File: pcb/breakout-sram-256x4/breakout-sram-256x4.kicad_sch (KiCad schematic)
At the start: 16 parts, among them U1 IS61WV25616-10TLI, U2 IS61WV25616-10TLI, U3 IS61WV25616-10TLI, U4 IS61WV25616-10TLI

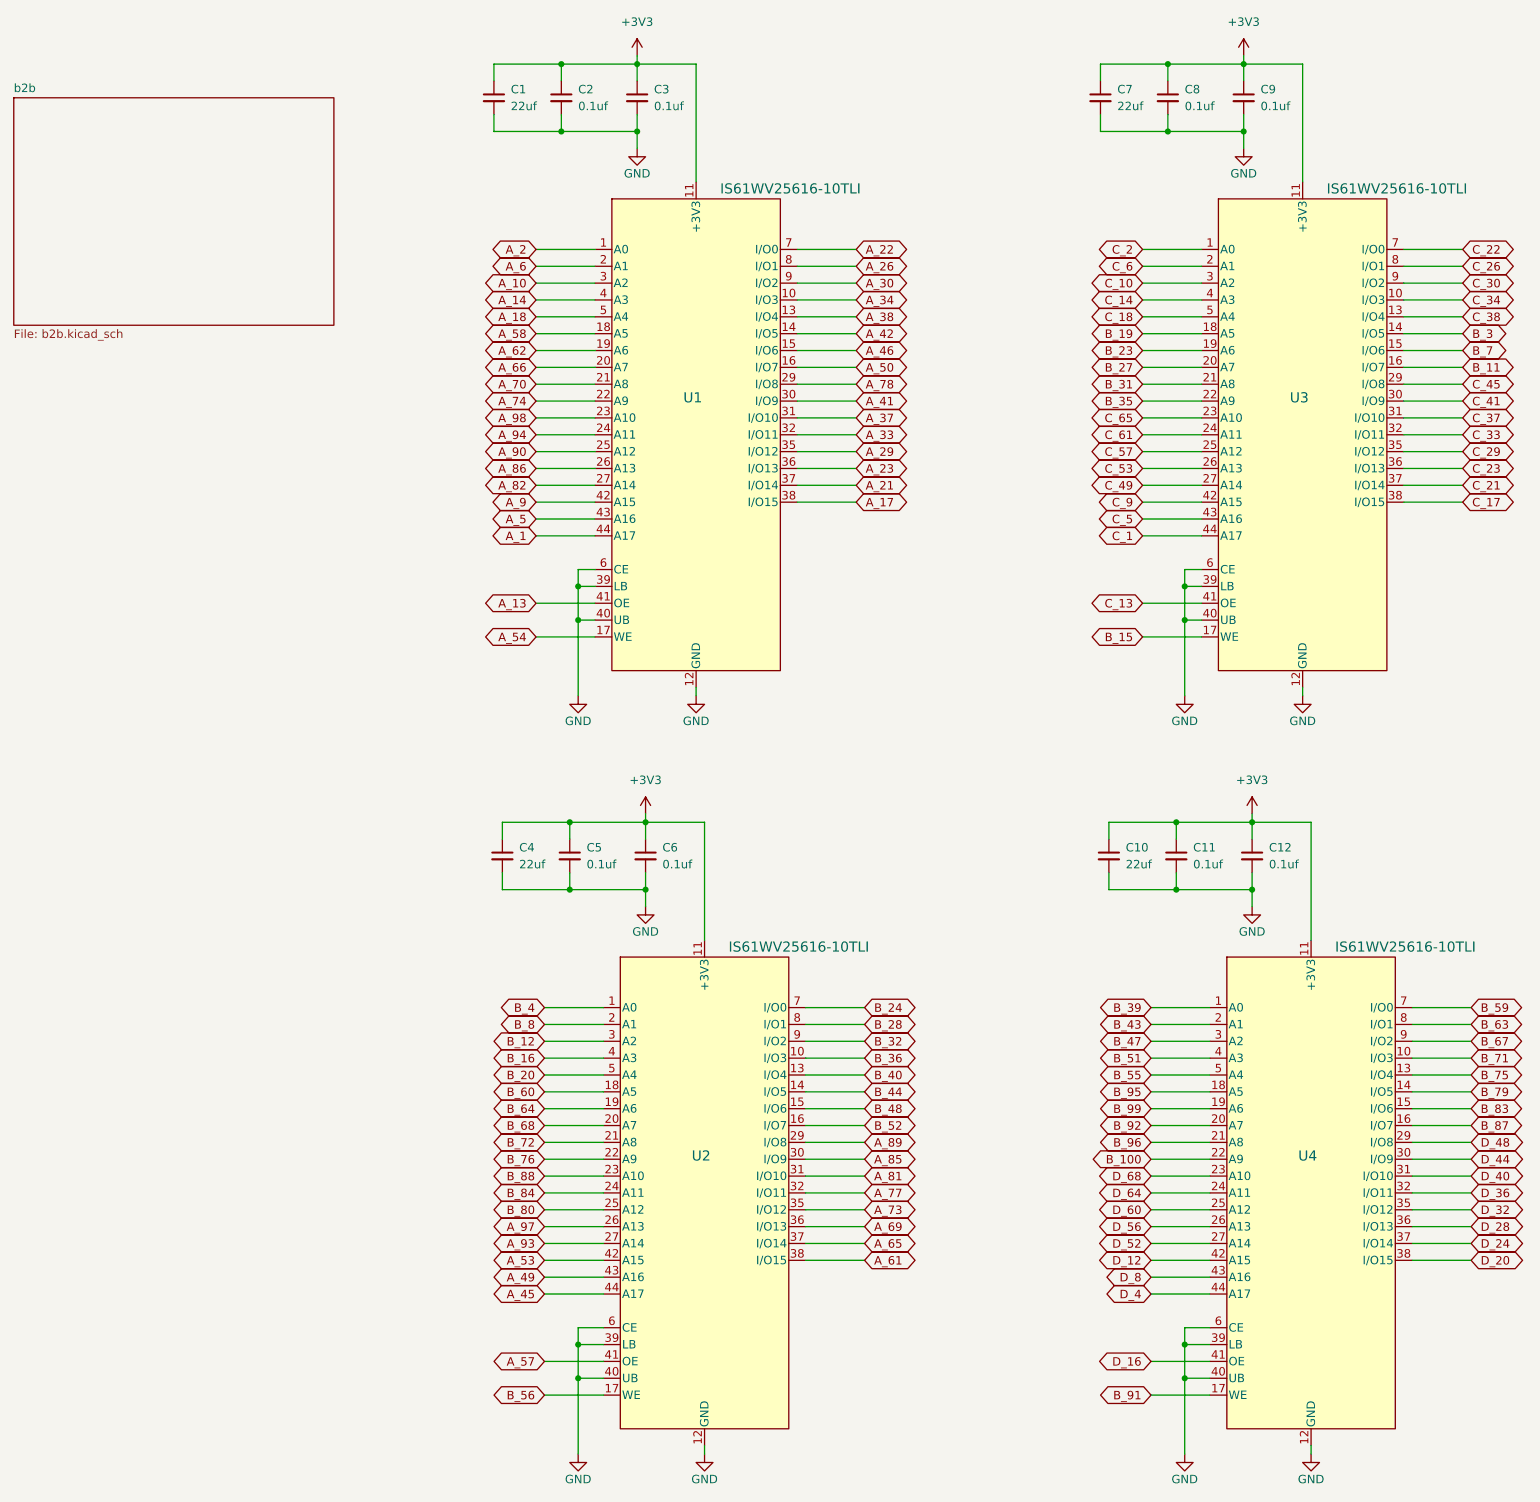
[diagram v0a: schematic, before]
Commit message: [sram_4x][pcb] make each sram ce settable with 0 ohm 603s
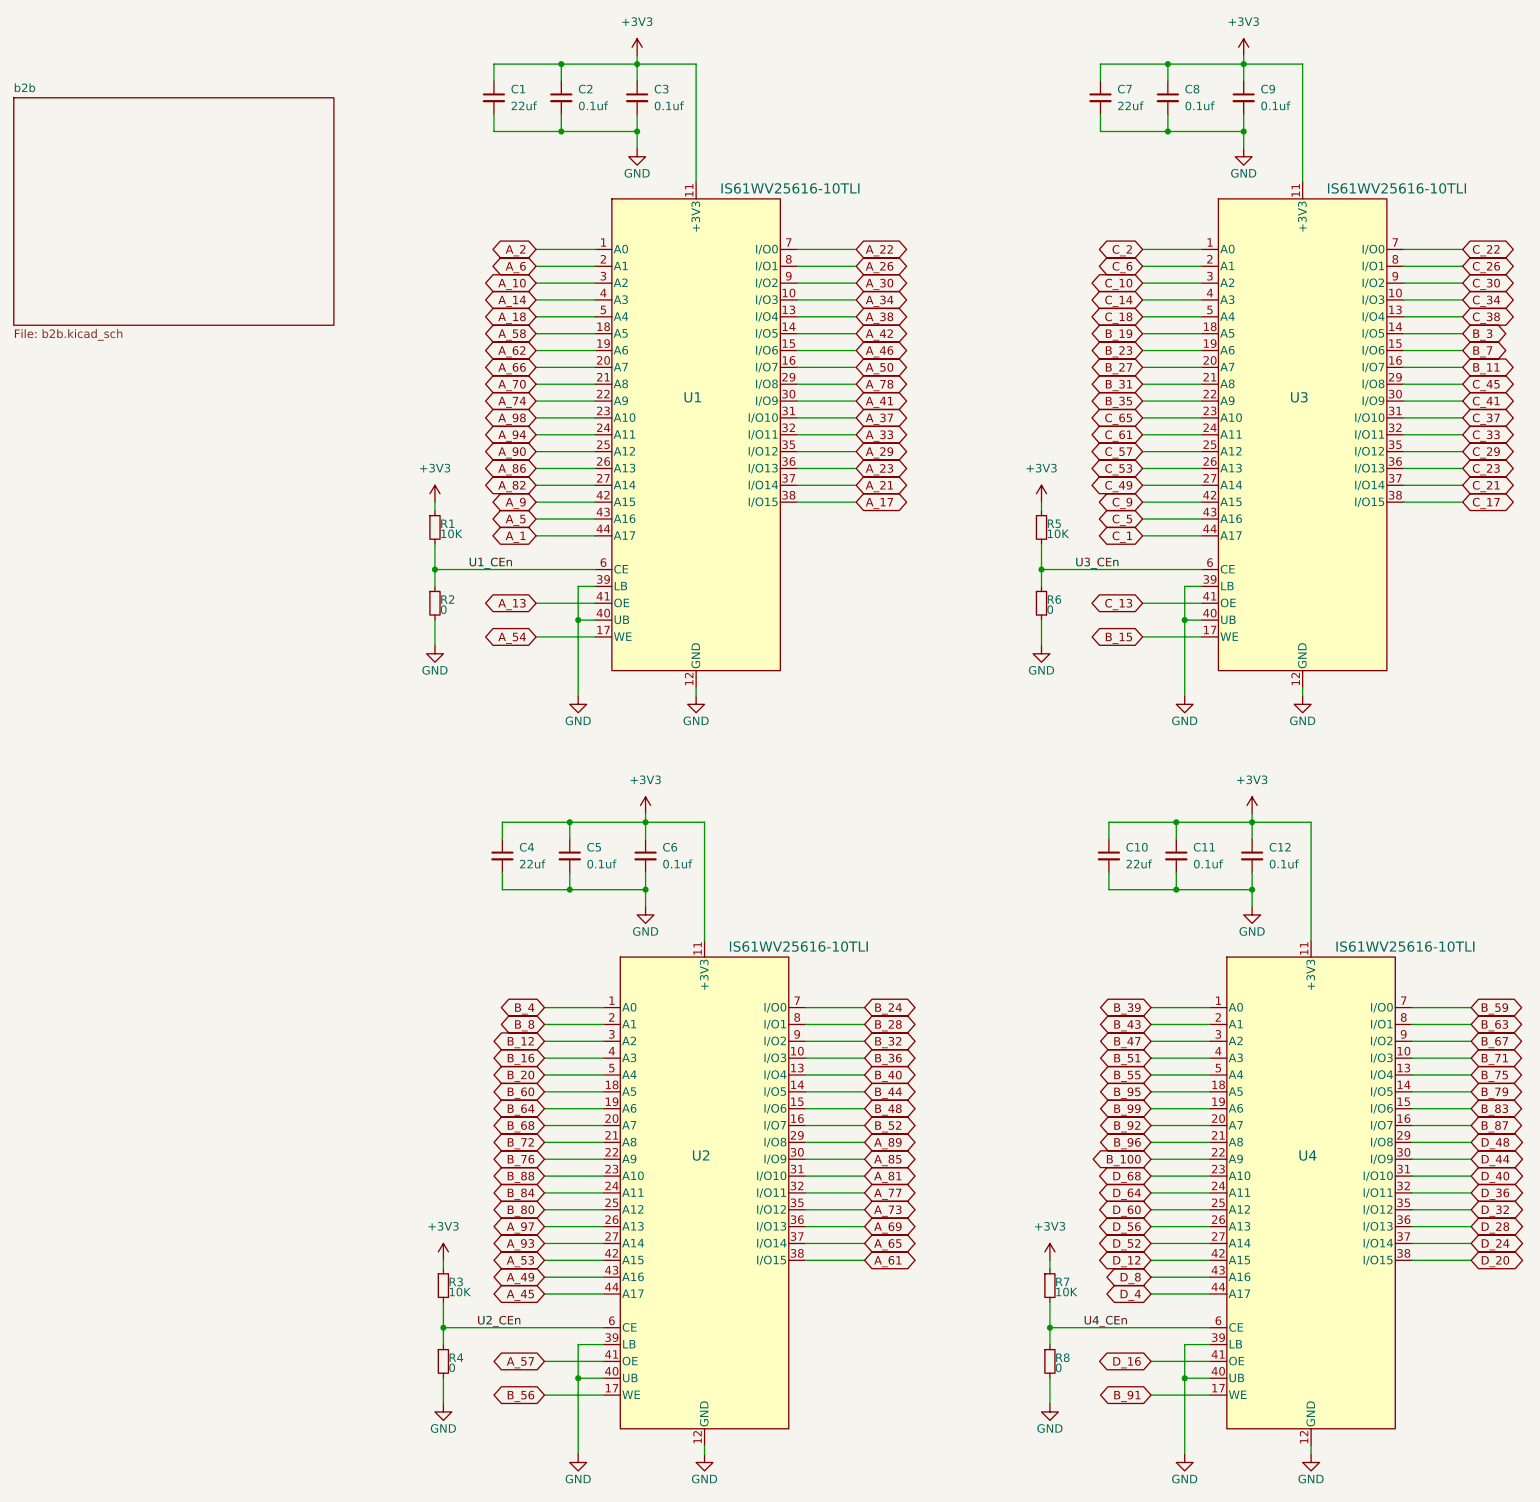
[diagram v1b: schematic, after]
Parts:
- added R1, R3, R5, R7: 10K, Resistor_SMD:R_0603_1608Metric, symbol Device:R_Small
- added R2, R4, R6, R8: 0, Resistor_SMD:R_0603_1608Metric, symbol Device:R_Small
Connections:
- net +3V3: now also R1.1, R3.1, R5.1, R7.1
- net GND: now also R2.2, R4.2, R6.2, R8.2; no longer U1.6 (CE), U2.6 (CE), U3.6 (CE), U4.6 (CE)
- new net U1_CEn: R1.2, R2.1, U1.6 (CE)
- new net U2_CEn: R3.2, R4.1, U2.6 (CE)
- new net U3_CEn: R5.2, R6.1, U3.6 (CE)
- new net U4_CEn: R7.2, R8.1, U4.6 (CE)

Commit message: [sram_4x][pcb] do not use nc from ice40
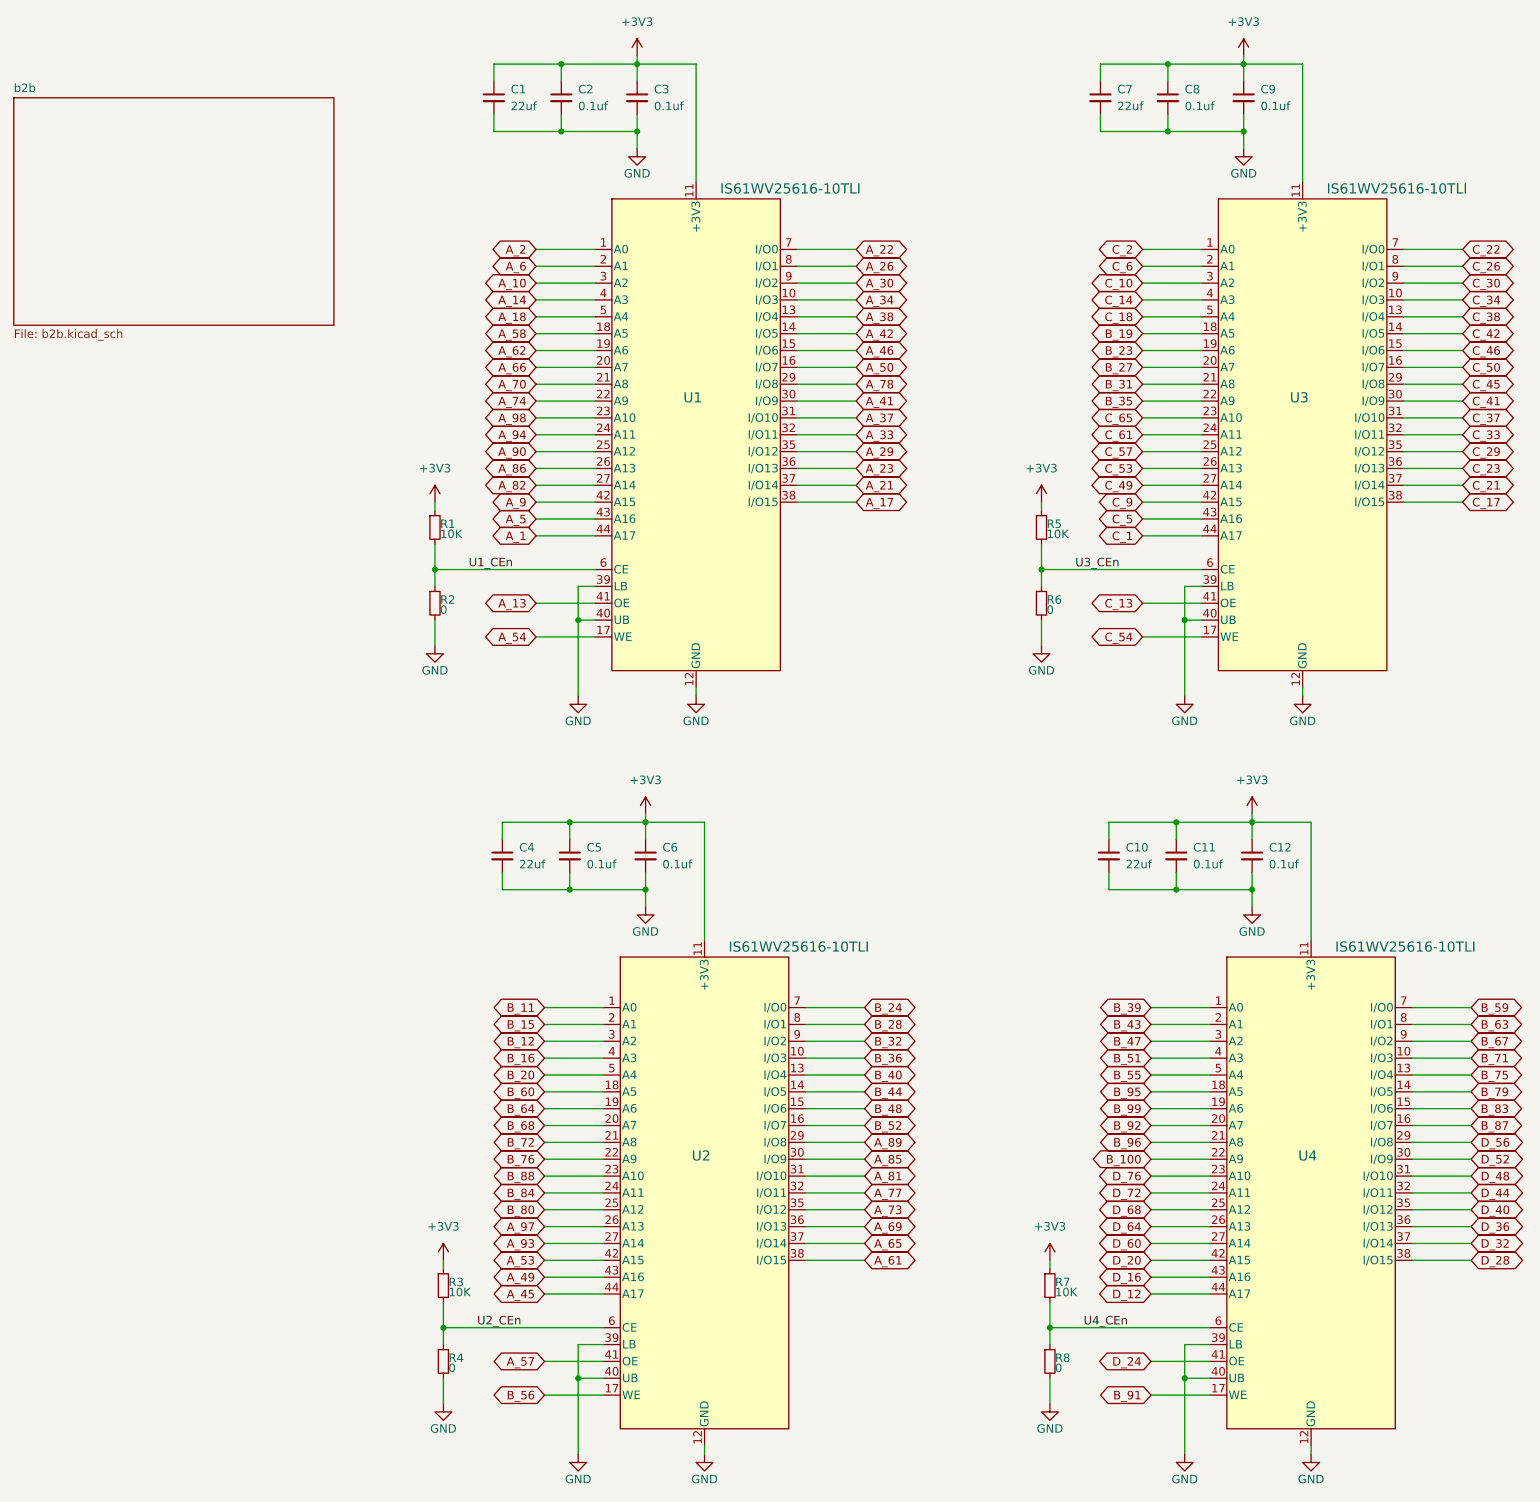
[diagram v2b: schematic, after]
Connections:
- net B_4 is gone; now on net B_11: U2.1 (A0)
- net B_8 is gone; now on net B_15: U2.2 (A1)
- net D_4 is gone; now on net D_12: U4.44 (A17)
- net D_8 is gone; now on net D_16: U4.43 (A16)
- net B_11: no longer U3.16 (I/O7)
- net B_15: no longer U3.17 (WE)
- net D_12: no longer U4.42 (A15)
- net D_16: no longer U4.41 (OE)
- net D_20: now also U4.42 (A15); no longer U4.38 (I/O15)
- net D_24: now also U4.41 (OE); no longer U4.37 (I/O14)
- net D_28: now also U4.38 (I/O15); no longer U4.36 (I/O13)
- net D_32: now also U4.37 (I/O14); no longer U4.35 (I/O12)
- net D_36: now also U4.36 (I/O13); no longer U4.32 (I/O11)
- net D_40: now also U4.35 (I/O12); no longer U4.31 (I/O10)
- net D_44: now also U4.32 (I/O11); no longer U4.30 (I/O9)
- net D_48: now also U4.31 (I/O10); no longer U4.29 (I/O8)
- net D_52: now also U4.30 (I/O9); no longer U4.27 (A14)
- net D_56: now also U4.29 (I/O8); no longer U4.26 (A13)
- net D_60: now also U4.27 (A14); no longer U4.25 (A12)
- net D_64: now also U4.26 (A13); no longer U4.24 (A11)
- net D_68: now also U4.25 (A12); no longer U4.23 (A10)
- net B_3 renamed C_42
- net B_7 renamed C_46
- new net C_50: U3.16 (I/O7)
- new net C_54: U3.17 (WE)
- new net D_72: U4.24 (A11)
- new net D_76: U4.23 (A10)

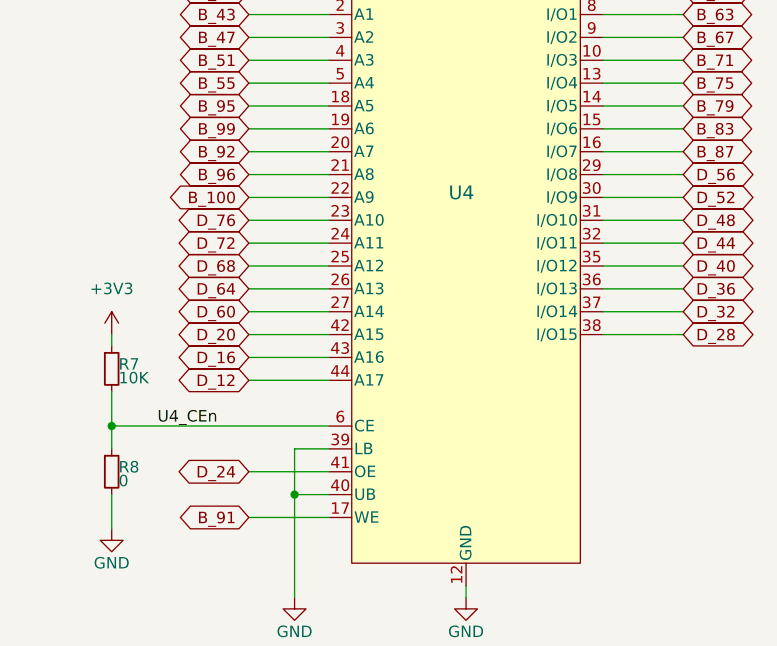
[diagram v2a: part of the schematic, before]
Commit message: [sram_4x][pcb] use bottom of lower right bank
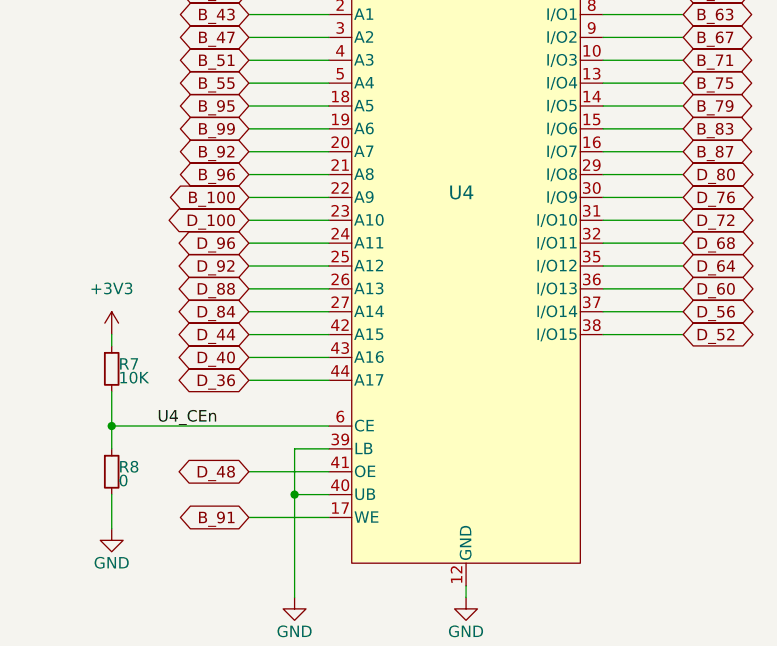
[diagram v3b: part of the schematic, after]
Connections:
- net D_12 is gone; now on net D_36: U4.44 (A17)
- net D_16 is gone; now on net D_40: U4.43 (A16)
- net D_20 is gone; now on net D_44: U4.42 (A15)
- net D_24 is gone; now on net D_48: U4.41 (OE)
- net D_28 is gone; now on net D_52: U4.38 (I/O15)
- net D_32 is gone; now on net D_56: U4.37 (I/O14)
- net D_36: no longer U4.36 (I/O13)
- net D_40: no longer U4.35 (I/O12)
- net D_44: no longer U4.32 (I/O11)
- net D_48: no longer U4.31 (I/O10)
- net D_52: no longer U4.30 (I/O9)
- net D_56: no longer U4.29 (I/O8)
- net D_60: now also U4.36 (I/O13); no longer U4.27 (A14)
- net D_64: now also U4.35 (I/O12); no longer U4.26 (A13)
- net D_68: now also U4.32 (I/O11); no longer U4.25 (A12)
- net D_72: now also U4.31 (I/O10); no longer U4.24 (A11)
- net D_76: now also U4.30 (I/O9); no longer U4.23 (A10)
- new net D_100: U4.23 (A10)
- new net D_80: U4.29 (I/O8)
- new net D_84: U4.27 (A14)
- new net D_88: U4.26 (A13)
- new net D_92: U4.25 (A12)
- new net D_96: U4.24 (A11)

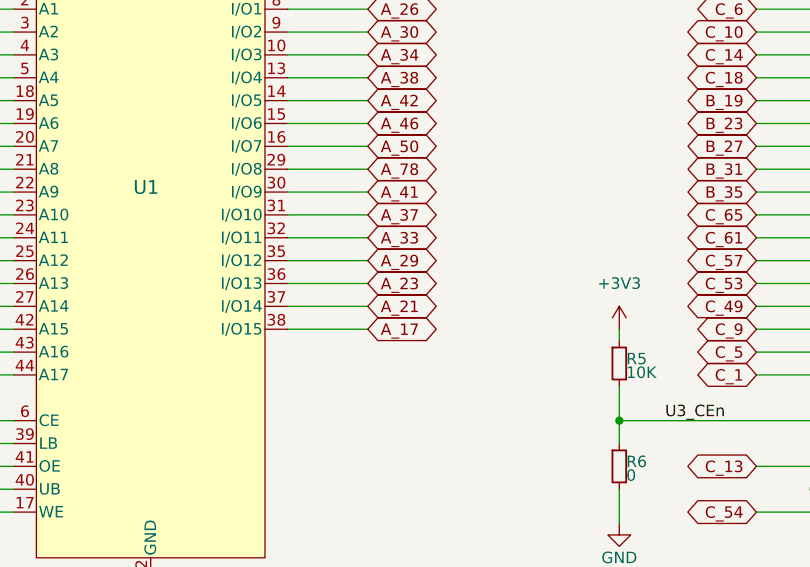
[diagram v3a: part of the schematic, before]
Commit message: [sram_4x][pcb] fix A_25 net label
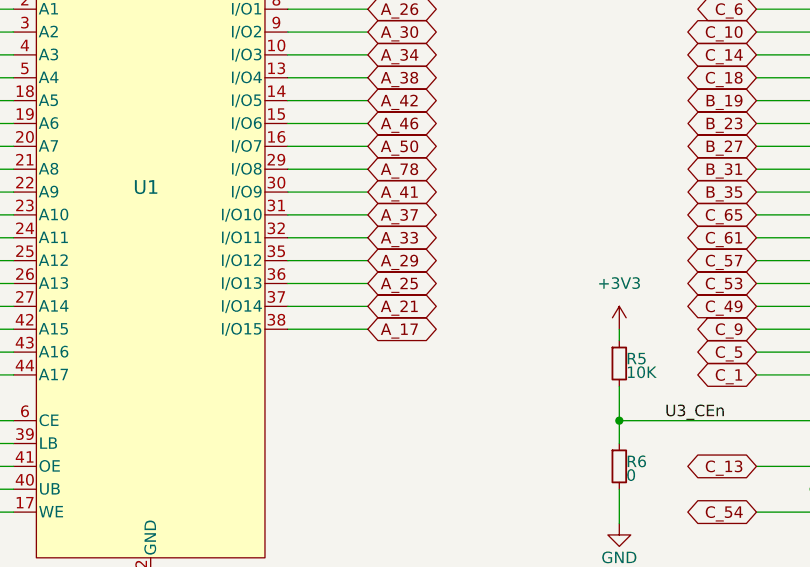
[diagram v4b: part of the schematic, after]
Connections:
- net A_23 renamed A_25
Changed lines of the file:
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@@
 (kicad_sch
-	(version 20231120)
+	(version 20250114)
 	(generator "eeschema")
-	(generator_version "8.0")
+	(generator_version "9.0")
 	(paper "USLedger")
 	(junction
@@
 	(label "U3_CEn"
 		(at 205.74 110.49 0)
-		(fields_autoplaced yes)
 		(effects
 			(font
@@
 	(label "U2_CEn"
 		(at 115.57 224.79 0)
-		(fields_autoplaced yes)
 		(effects
 			(font
@@
 	(label "U4_CEn"
 		(at 207.01 224.79 0)
-		(fields_autoplaced yes)
 		(effects
 			(font
@@
 	(label "U1_CEn"
 		(at 114.3 110.49 0)
-		(fields_autoplaced yes)
 		(effects
 			(font
@@
 		)
 	)
-	(global_label "A_23"
+	(global_label "A_25"
 		(shape bidirectional)
 		(at 172.72 95.25 0)
@@
 		(at 45.72 39.37)
 		(size 48.26 34.29)
+		(exclude_from_sim no)
+		(in_bom yes)
+		(on_board yes)
+		(dnp no)
 		(fields_autoplaced yes)
 		(stroke
@@
 		)
 	)
+	(embedded_fonts no)
 )
